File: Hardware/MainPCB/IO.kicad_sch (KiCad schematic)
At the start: 9 parts, among them J1 Conn_Coaxial, J2 Conn_Coaxial, J3 Conn_Coaxial, J4 Conn_Coaxial, J5 Conn_Coaxial, J6 DB15_Female_HighDensity_Mount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, J7 AudioJack3, J8 Conn_01x21_Male, J9 Conn_01x21_Male

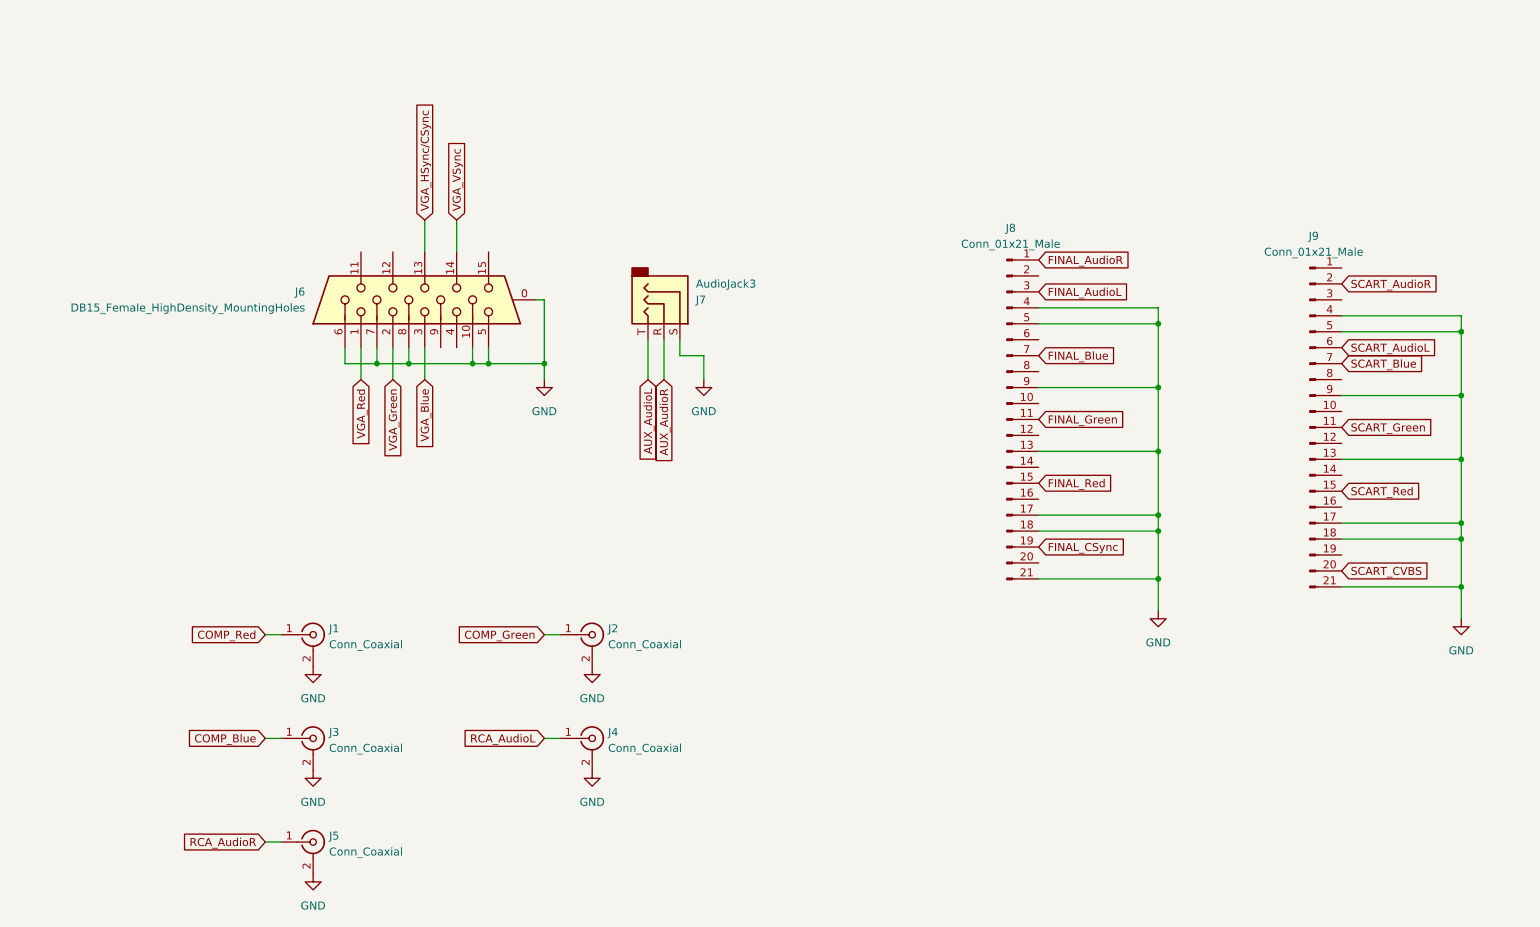
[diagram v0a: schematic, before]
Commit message: Fixed color bending issue; Added diagnostics
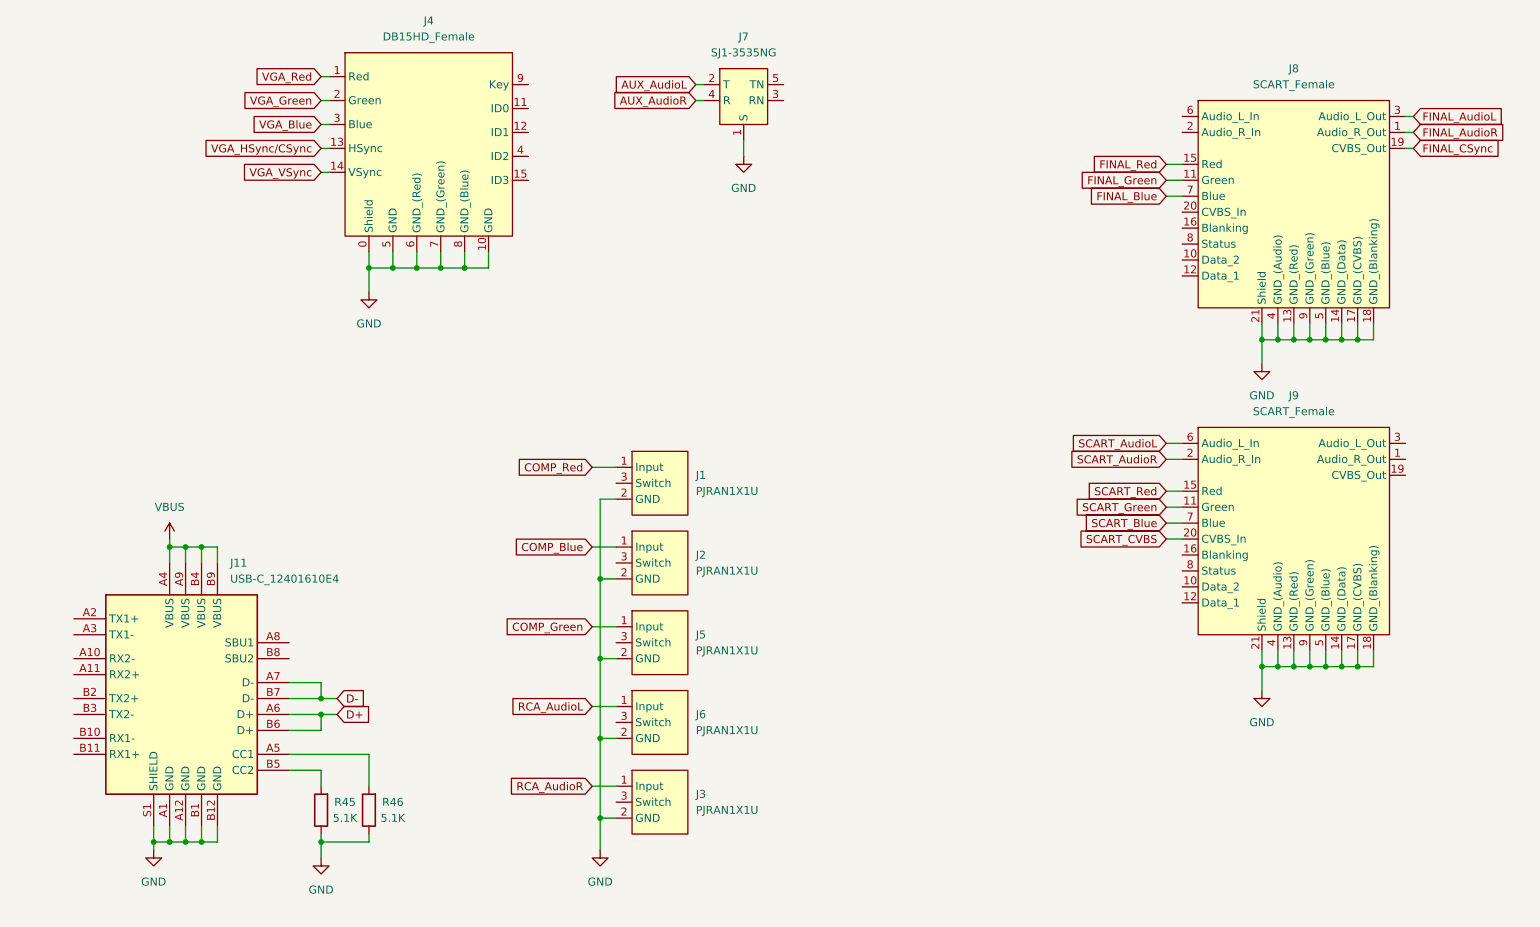
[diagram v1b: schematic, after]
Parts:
- removed J1, J2, J3, J4, J5: Conn_Coaxial, Mouser:PJRAN1X1U02AUX, symbol Connector:Conn_Coaxial
- removed J6: DB15_Female_HighDensity_MountingHoles, Mouser:L77HDE15SD1CH4RHNVGA, symbol Connector:DB15_Female_HighDensity_MountingHoles
- removed J7: AudioJack3, Connector_Audio:Jack_3.5mm_CUI_SJ1-3535NG_Horizontal, symbol Connector:AudioJack3
- removed J8, J9: Conn_01x21_Male, AE:SCART, symbol Connector:Conn_01x21_Male
- added J1, J2, J3, J5, J6: PJRAN1X1U, RT5XP-EXP:PJRAN1X1U, symbol RT5XP_EXP:PJRAN1X1U
- added J11: USB-C_12401610E4, RT5XP-EXP:USB-C_12401610E4, symbol RT5XP_EXP:USB-C_12401610E4
- added J4: DB15HD_Female, RT5XP-EXP:77HDE15SD1CH4RHNVGA, symbol RT5XP_EXP:DB15HD_Female
- added J7: SJ1-3535NG, RT5XP-EXP:SJ1-3535NG, symbol RT5XP_EXP:SJ1-3535NG
- added J8, J9: SCART_Female, RT5XP-EXP:SCART_Female, symbol RT5XP_EXP:SCART_Female
- added R45, R46: 5.1K, RT5XP-EXP:R_0603, symbol RT5XP_EXP:R
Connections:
- net AUX_AudioL: now also J7.2 (T)
- net AUX_AudioR: now also J7.4 (R)
- net COMP_Blue: now also J2.1 (Input)
- net COMP_Green: now also J5.1 (Input)
- net COMP_Red: now also J1.1 (Input)
- net FINAL_AudioL: now also J8.3 (Audio_L_Out)
- net FINAL_AudioR: now also J8.1 (Audio_R_Out)
- net FINAL_Blue: now also J8.7 (Blue)
- net FINAL_CSync: now also J8.19 (CVBS_Out)
- net FINAL_Green: now also J8.11 (Green)
- net FINAL_Red: now also J8.15 (Red)
- net GND: now also J1.2 (GND), J11.A1 (GND), J11.A12 (GND), J11.B1 (GND), J11.B12 (GND), J11.S1 (SHIELD), J2.2 (GND), J3.2 (GND), J4.0 (Shield), J4.10 (GND), J4.5 (GND), J4.6 (GND_(Red)), J4.7 (GND_(Green)), J4.8 (GND_(Blue)), J5.2 (GND), J6.2 (GND), J7.1 (S), J8.13 (GND_(Red)), J8.14 (GND_(Data)), J8.17 (GND_(CVBS)), J8.18 (GND_(Blanking)), J8.21 (Shield), J8.4 (GND_(Audio)), J8.5 (GND_(Blue)), J8.9 (GND_(Green)), J9.13 (GND_(Red)), J9.14 (GND_(Data)), J9.17 (GND_(CVBS)), J9.18 (GND_(Blanking)), J9.21 (Shield), J9.4 (GND_(Audio)), J9.5 (GND_(Blue)), J9.9 (GND_(Green)), R45.1, R46.1
- net RCA_AudioL: now also J6.1 (Input)
- net RCA_AudioR: now also J3.1 (Input)
- net SCART_AudioL: now also J9.6 (Audio_L_In)
- net SCART_AudioR: now also J9.2 (Audio_R_In)
- net SCART_Blue: now also J9.7 (Blue)
- net SCART_CVBS: now also J9.20 (CVBS_In)
- net SCART_Green: now also J9.11 (Green)
- net SCART_Red: now also J9.15 (Red)
- net VGA_Blue: now also J4.3 (Blue)
- net VGA_Green: now also J4.2 (Green)
- net VGA_HSync/CSync: now also J4.13 (HSync)
- net VGA_Red: now also J4.1 (Red)
- net VGA_VSync: now also J4.14 (VSync)
- new net: J11.A5 (CC1), R46.2
- new net: J11.B5 (CC2), R45.2
- new net D+: J11.A6 (D+), J11.B6 (D+)
- new net D-: J11.A7 (D-), J11.B7 (D-)
- new net VBUS: J11.A4 (VBUS), J11.A9 (VBUS), J11.B4 (VBUS), J11.B9 (VBUS)
